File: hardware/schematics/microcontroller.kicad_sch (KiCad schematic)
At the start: 3 parts, among them U3 ESP32-C3-WROOM-02

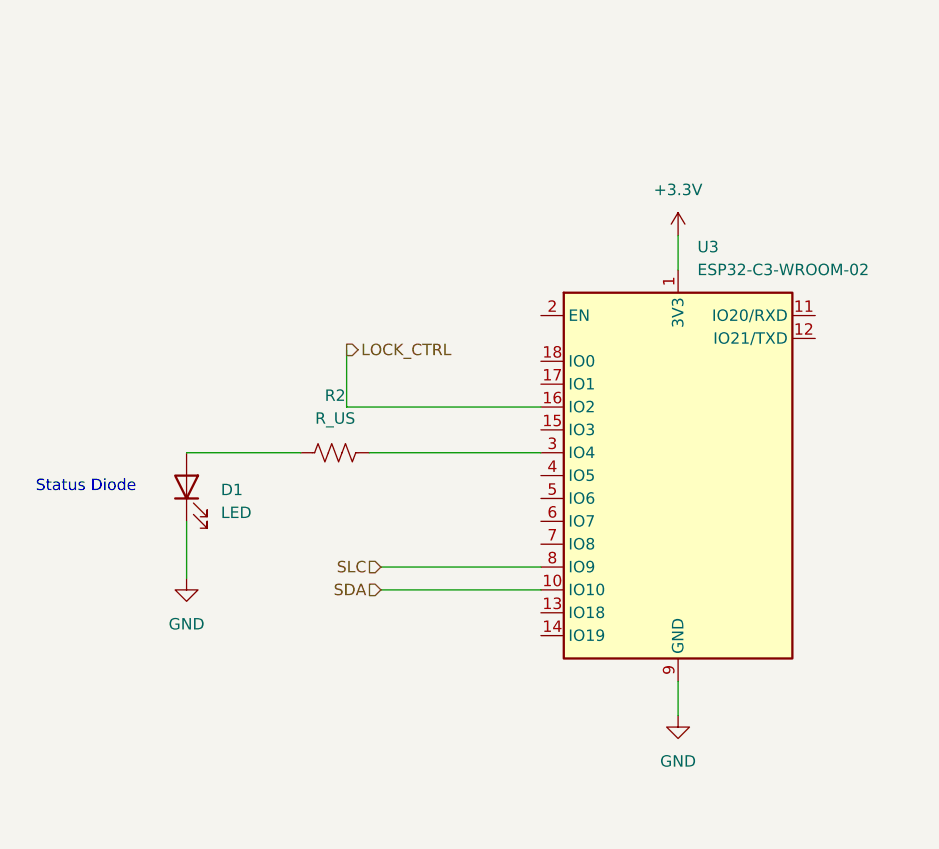
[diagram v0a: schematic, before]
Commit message: added header file (config.h) to esp32 source code to make it look cleaner. Will add more header files in future. Edited schematic - not finished. Switched board from esp32-s3-devkit-c1 to esp32-devkit-v1, since Serial Monitor seems to only work with the second one. Updated .ini file in pio to match
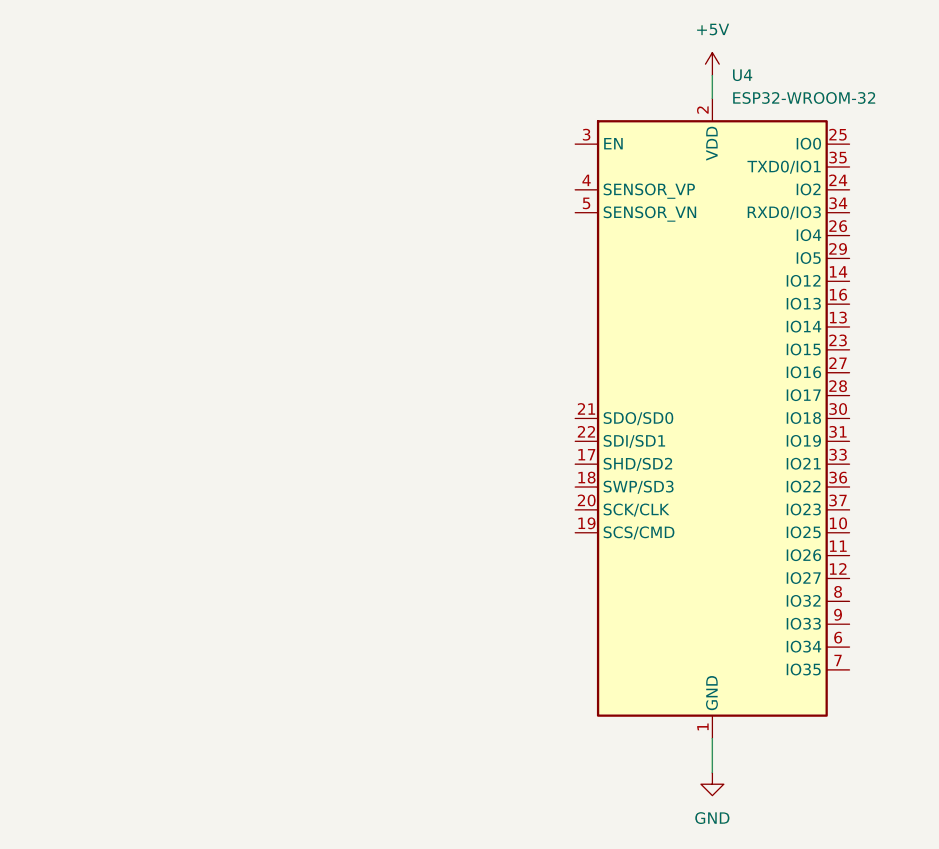
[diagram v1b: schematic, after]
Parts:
- removed D1: LED, symbol Device:LED
- removed R2: R_US, symbol Device:R_US
- removed U3: ESP32-C3-WROOM-02, RF_Module:ESP32-C3-WROOM-02, symbol RF_Module:ESP32-C3-WROOM-02
- added U4: ESP32-WROOM-32, RF_Module:ESP32-WROOM-32, symbol RF_Module:ESP32-WROOM-32
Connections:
- net GND: now also U4.1 (GND), U4.15 (GND), U4.38 (GND), U4.39 (GND)
- new net +5V: U4.2 (VDD)
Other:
- note removed: "Status Diode"
